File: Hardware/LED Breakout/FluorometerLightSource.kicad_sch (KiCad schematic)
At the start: 31 parts, among them Q1 BSS214NW, Q2 BSS214NW, Q3 BSS214NW, Q4 BSS214NW, Q5 BSS214NW, Q6 BSS214NW, Q7 BSS214NW, Q8 BSS214NW

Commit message: Layout updated for LEDs and Science Sensor Board, schematic for CCD
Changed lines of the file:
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@@
     (pin "2")
-  )
-  (symbol (lib_id "power:+12V") (at 241.3 22.86 0) (mirror y) (unit 1)
-    (in_bom yes) (on_board yes) (fields_autoplaced)
-    (property "Reference" "#PWR08" (id 0) (at 241.3 26.67 0)
-      (effects (font (size 1.27 1.27)) hide)
-    )
-    (property "Value" "+12V" (id 1) (at 241.3 19.2842 0))
-    (property "Footprint" "" (id 2) (at 241.3 22.86 0)
-      (effects (font (size 1.27 1.27)) hide)
-    )
-    (property "Datasheet" "" (id 3) (at 241.3 22.86 0)
-      (effects (font (size 1.27 1.27)) hide)
-    )
-    (pin "1")
   )
   (symbol (lib_id "Device:LED") (at 182.88 28.575 90) (unit 1)
@@
     (pin "3")
   )
+  (symbol (lib_id "power:GND") (at 257.175 59.055 0) (mirror y) (unit 1)
+    (in_bom yes) (on_board yes) (fields_autoplaced)
+    (property "Reference" "#PWR0102" (id 0) (at 257.175 65.405 0)
+      (effects (font (size 1.27 1.27)) hide)
+    )
+    (property "Value" "GND" (id 1) (at 257.175 63.4984 0))
+    (property "Footprint" "" (id 2) (at 257.175 59.055 0)
+      (effects (font (size 1.27 1.27)) hide)
+    )
+    (property "Datasheet" "" (id 3) (at 257.175 59.055 0)
+      (effects (font (size 1.27 1.27)) hide)
+    )
+    (pin "1")
+  )
   (symbol (lib_id "MRDT_Drill_Holes:Via") (at 125.095 22.86 0) (unit 1)
     (in_bom yes) (on_board yes)
@@
     (pin "3")
   )
-  (symbol (lib_id "power:GND") (at 257.175 59.055 0) (mirror y) (unit 1)
-    (in_bom yes) (on_board yes) (fields_autoplaced)
-    (property "Reference" "#PWR010" (id 0) (at 257.175 65.405 0)
-      (effects (font (size 1.27 1.27)) hide)
-    )
-    (property "Value" "GND" (id 1) (at 257.175 63.4984 0))
-    (property "Footprint" "" (id 2) (at 257.175 59.055 0)
-      (effects (font (size 1.27 1.27)) hide)
-    )
-    (property "Datasheet" "" (id 3) (at 257.175 59.055 0)
-      (effects (font (size 1.27 1.27)) hide)
-    )
-    (pin "1")
-  )
   (symbol (lib_id "Device:LED") (at 162.56 28.575 90) (unit 1)
     (in_bom yes) (on_board yes) (fields_autoplaced)
@@
     (pin "1")
     (pin "2")
+  )
+  (symbol (lib_id "power:+12V") (at 241.3 22.86 0) (unit 1)
+    (in_bom yes) (on_board yes) (fields_autoplaced)
+    (property "Reference" "#PWR0104" (id 0) (at 241.3 26.67 0)
+      (effects (font (size 1.27 1.27)) hide)
+    )
+    (property "Value" "+12V" (id 1) (at 241.3 19.2842 0))
+    (property "Footprint" "" (id 2) (at 241.3 22.86 0)
+      (effects (font (size 1.27 1.27)) hide)
+    )
+    (property "Datasheet" "" (id 3) (at 241.3 22.86 0)
+      (effects (font (size 1.27 1.27)) hide)
+    )
+    (pin "1")
   )
   (symbol (lib_id "Transistor_FET:BSS214NW") (at 175.26 64.77 0) (mirror y) (unit 1)
@@
       (reference "#PWR07") (unit 1) (value "GND") (footprint "")
     )
-    (path "/5bb108ea-f852-4bb6-a76c-59e8eadda8cc"
-      (reference "#PWR08") (unit 1) (value "+12V") (footprint "")
-    )
     (path "/47fd6be5-fa60-4635-b771-4014139ebb0a"
       (reference "#PWR09") (unit 1) (value "GND") (footprint "")
     )
-    (path "/b1ec8728-b864-483d-bc0c-76204a7033f4"
-      (reference "#PWR010") (unit 1) (value "GND") (footprint "")
-    )
     (path "/46c7e2d7-b987-409e-8126-3b8624c4a8a5"
       (reference "#PWR0101") (unit 1) (value "+12V") (footprint "")
     )
+    (path "/84e6c645-bb8c-47ca-a548-635f2687c75a"
+      (reference "#PWR0102") (unit 1) (value "GND") (footprint "")
+    )
     (path "/6af26e63-c3a7-47c3-b29f-c6d6b718038b"
       (reference "#PWR0103") (unit 1) (value "GND") (footprint "")
     )
+    (path "/ca04740c-a1a8-4469-8aab-3476a5e676a7"
+      (reference "#PWR0104") (unit 1) (value "+12V") (footprint "")
+    )
     (path "/ad0a8dc5-e5b8-45f3-9299-b7bfa32c3093"

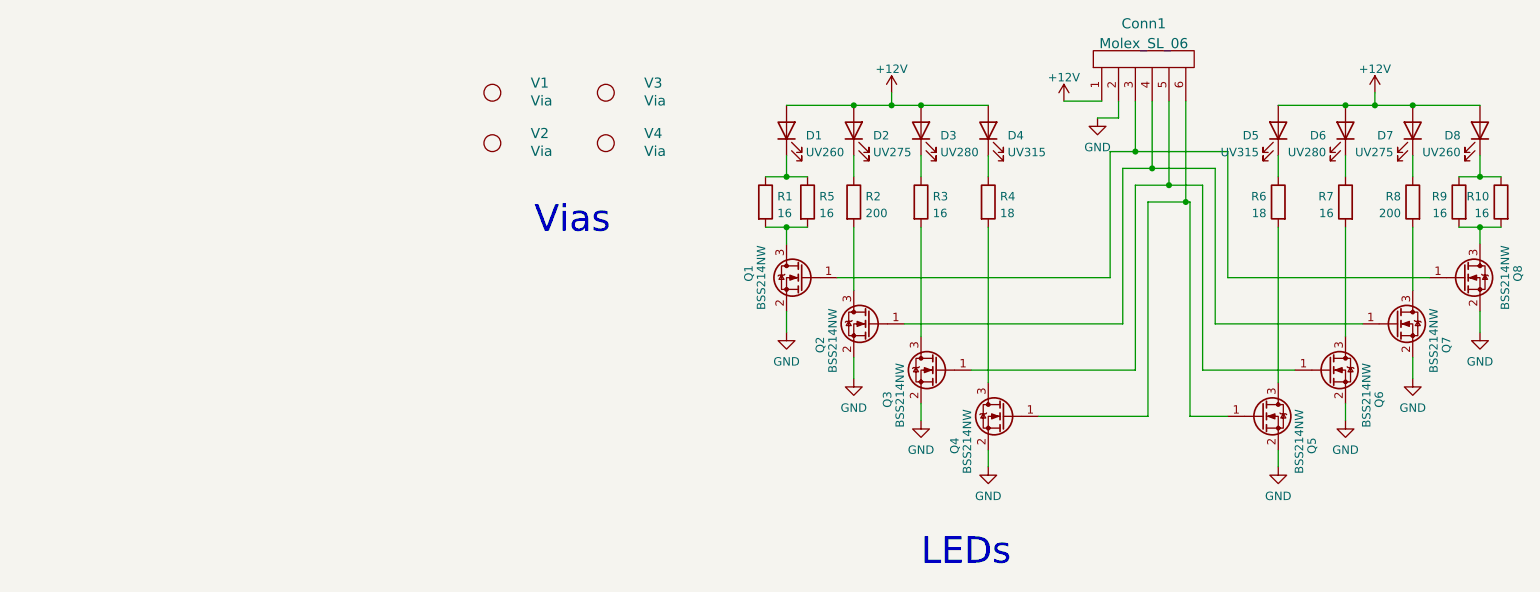
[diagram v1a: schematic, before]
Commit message: Added indicators to LED breakout + made gerbs
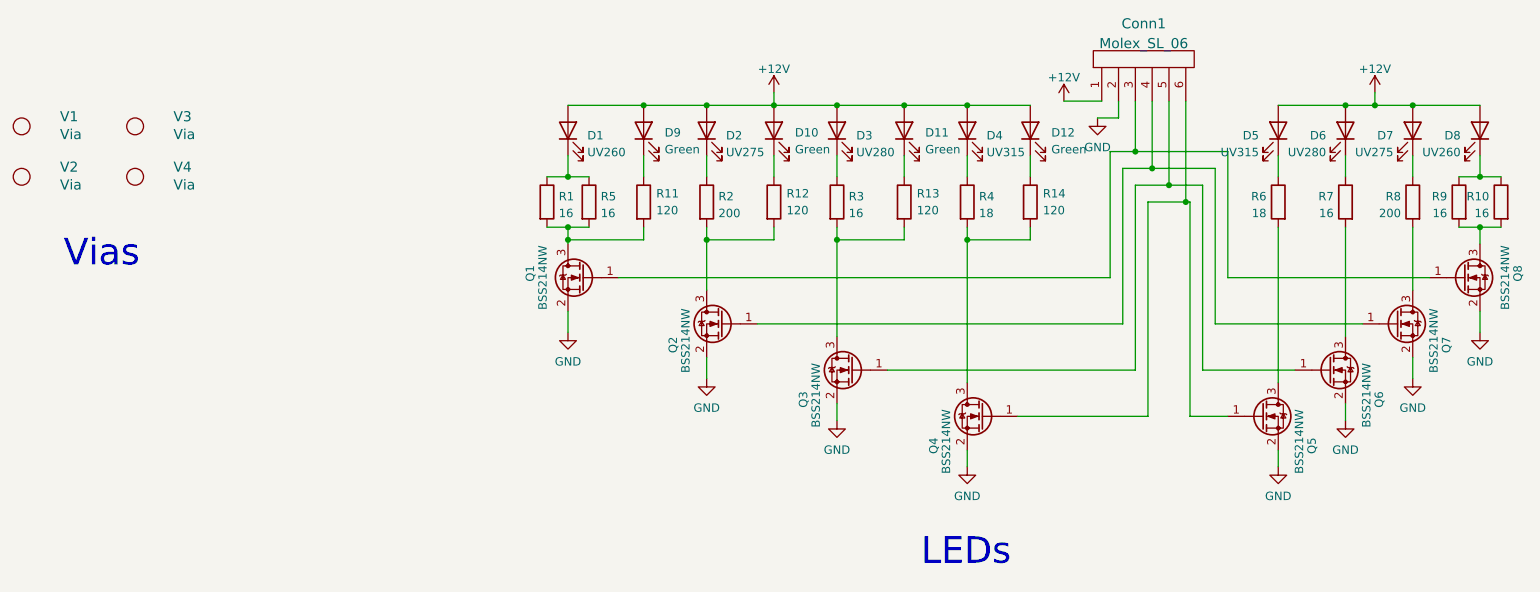
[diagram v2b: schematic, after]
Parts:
- added D10, D11, D12, D9: Green, LED_SMD:LED_0603_1608Metric_Pad1.05x0.95mm_HandSolder, symbol Device:LED
- added R11, R12, R13, R14: 120, Resistor_SMD:R_0603_1608Metric_Pad0.98x0.95mm_HandSolder, symbol Device:R
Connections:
- net +12V: now also D10.2 (A), D11.2 (A), D12.2 (A), D9.2 (A)
- net at Q2.3 (D), R2.2: now also R12.2
- net at Q4.3 (D), R4.2: now also R14.2
- net at Q1.3 (D), R1.2, R5.2: now also R11.2
- net at Q3.3 (D), R3.2: now also R13.2
- new net: D12.1 (K), R14.1
- new net: D9.1 (K), R11.1
- new net: D11.1 (K), R13.1
- new net: D10.1 (K), R12.1
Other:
- moved on the sheet: D1, D2, D3, D4, Q1, Q2, Q3, Q4, R1, R2, R3, R4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
